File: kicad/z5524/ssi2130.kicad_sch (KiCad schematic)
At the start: 50 parts, among them Q1 2N7002K, U1 TL072, U13 DG442xY, U2 SSI2130, U7 LM311

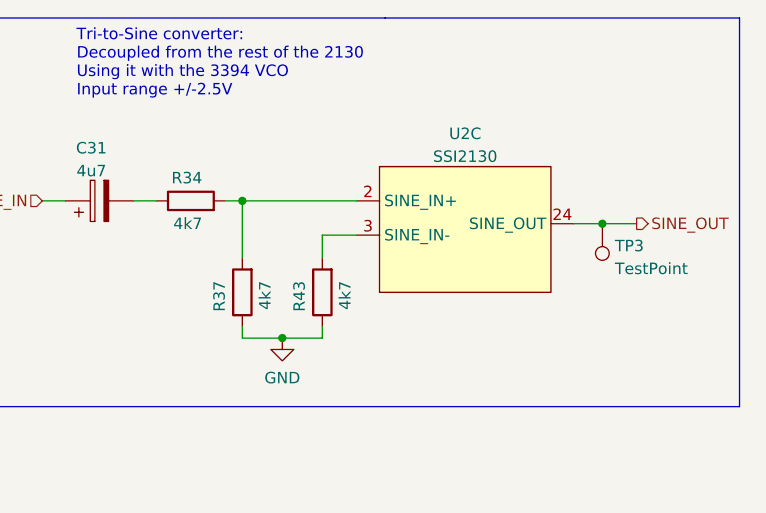
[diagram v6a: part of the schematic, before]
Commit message: silkscreen updates, offgrid resolved
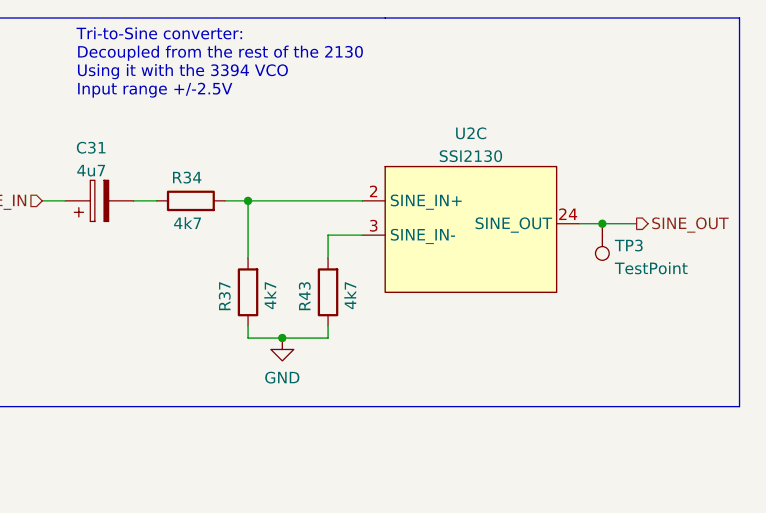
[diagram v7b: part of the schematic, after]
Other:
- moved on the sheet: R37, R43, U2C

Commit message: silkscreen looking better, some routing updates
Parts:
- U2: footprint Package_DFN_QFN:QFN-32-1EP_4x4mm_P0.4mm_EP2.65x2.65mm_Handsolder -> project_footprints:QFN-32-1EP_4x4mm_P0.4mm_EP2.65x2.65mm_Handsolder
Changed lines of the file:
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@@
       (effects (font (size 1.27 1.27)))
     )
-    (property "Footprint" "Package_DFN_QFN:QFN-32-1EP_4x4mm_P0.4mm_EP2.65x2.65mm_Handsolder" (at 227.33 135.89 0)
+    (property "Footprint" "project_footprints:QFN-32-1EP_4x4mm_P0.4mm_EP2.65x2.65mm_Handsolder" (at 227.33 135.89 0)
       (effects (font (size 1.27 1.27)) hide)
     )
@@
       (effects (font (size 1.27 1.27)) (justify left))
     )
-    (property "Footprint" "Package_DFN_QFN:QFN-32-1EP_4x4mm_P0.4mm_EP2.65x2.65mm_Handsolder" (at 41.91 226.06 0)
+    (property "Footprint" "project_footprints:QFN-32-1EP_4x4mm_P0.4mm_EP2.65x2.65mm_Handsolder" (at 41.91 226.06 0)
       (effects (font (size 1.27 1.27)) hide)
     )
@@
       (effects (font (size 1.27 1.27)) (justify left))
     )
-    (property "Footprint" "Package_DFN_QFN:QFN-32-1EP_4x4mm_P0.4mm_EP2.65x2.65mm_Handsolder" (at 270.51 63.5 0)
+    (property "Footprint" "project_footprints:QFN-32-1EP_4x4mm_P0.4mm_EP2.65x2.65mm_Handsolder" (at 270.51 63.5 0)
       (effects (font (size 1.27 1.27)) hide)
     )
@@
       (effects (font (size 1.27 1.27)))
     )
-    (property "Footprint" "Package_DFN_QFN:QFN-32-1EP_4x4mm_P0.4mm_EP2.65x2.65mm_Handsolder" (at 384.81 38.1 0)
-      (effects (font (size 1.27 1.27)) hide)
-    )
+    (property "Footprint" "project_footprints:QFN-32-1EP_4x4mm_P0.4mm_EP2.65x2.65mm_Handsolder" (at 384.81 38.1 0)
+      (effects (font (size 1.27 1.27)) hide)
+    )
